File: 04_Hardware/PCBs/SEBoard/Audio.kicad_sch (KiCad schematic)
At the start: 20 parts, among them J22 53047-0210, U1 SC200EEMNA-E53-UGNDA, U100 PAM8302AASCR

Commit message: feat(schematic): add SE250B4 symbol to schematic (unchecked)
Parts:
- removed TP49, TP50, TP51: VBAT, TestPoint:TestPoint_Pad_D1.0mm, symbol SEBoard:TestPoint
- removed U1: SC200EEMNA-E53-UGNDA, SEBoard:SC200E_SC206E, symbol SEBoard:SC200E
- added C108: 10pF 50V, 000MCLib:CAPC1005X55N, symbol 000MCLib:GRM1555C1H100JA01D
- added C109, C65, C99: 100nF 10V, 000MCLib:CAPC1005X55N, symbol 000MCLib:GRM155R71A104KA01D
- added C63: 33pF 50V, 000MCLib:CAPC1005X55N, symbol 000MCLib:GRM1555C1H330JA01D
- added FB3: 110Ohm 1200mA, 000MCLib:BEADC1005X55N, symbol 000MCLib:74269242111
- added MK1: CMM-3729AT-42316-TR, 000MCLib:CMM3729AT42316TR, symbol 000MCLib:CMM-3729AT-42316-TR
- added R102: 0R, 000MCLib:RC0402N_YAG, symbol 000MCLib:RC0402JR-070RL
- added U5: SE250B4, 000MCLib:XCVR_SE250B4-NA, symbol 000MCLib:SE250B4
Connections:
- net GND: now also C108.2, C109.2, C63.2, R102.2
- net at C100.1: now also U5.BD6 (CDC_AUX_P)
- net at C101.1: now also U5.BE5 (CDC_AUX_M)
- new net: C108.1, C65.2, MK1.4 (OUTPUT)
- new net: C99.2, MK1.2 (GND_1), MK1.3 (GND_2), R102.1
- new net: C109.1, FB3.1, MK1.1 (VDD)
- new net MIC1_M: C99.1, U5.BD8 (CDC_IN1_M)
- new net MIC1_P: C63.1, C65.1, U5.BC7 (CDC_IN1_P)
- new net MIC_BIAS1: FB3.2, U5.BC9 (CDC_MIC_BIAS1)
- no-connect marks 12 -> 17
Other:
- note added: "Mic"

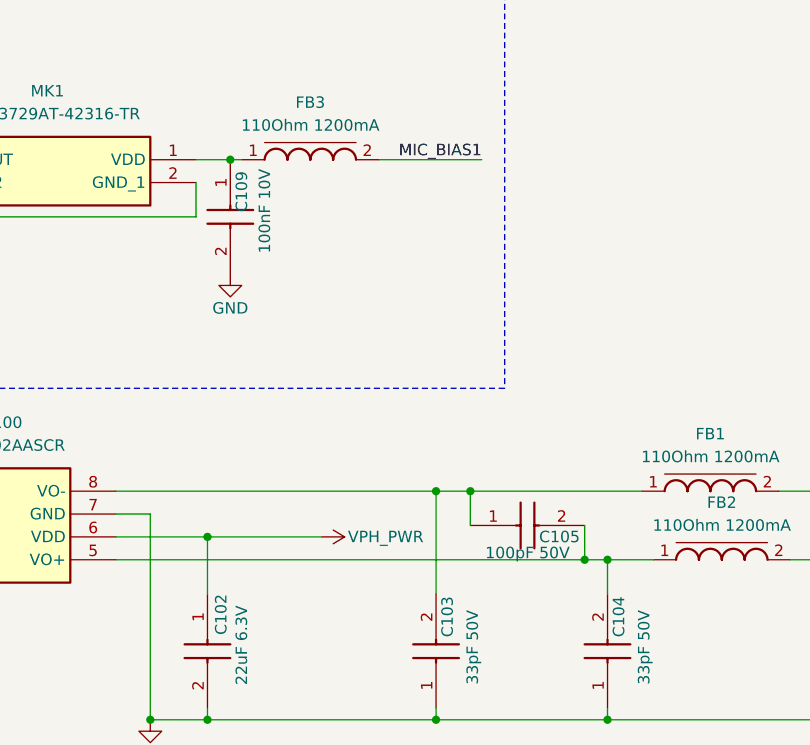
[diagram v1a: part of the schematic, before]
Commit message: feat: Updated schematic layout and moved new components to Layout
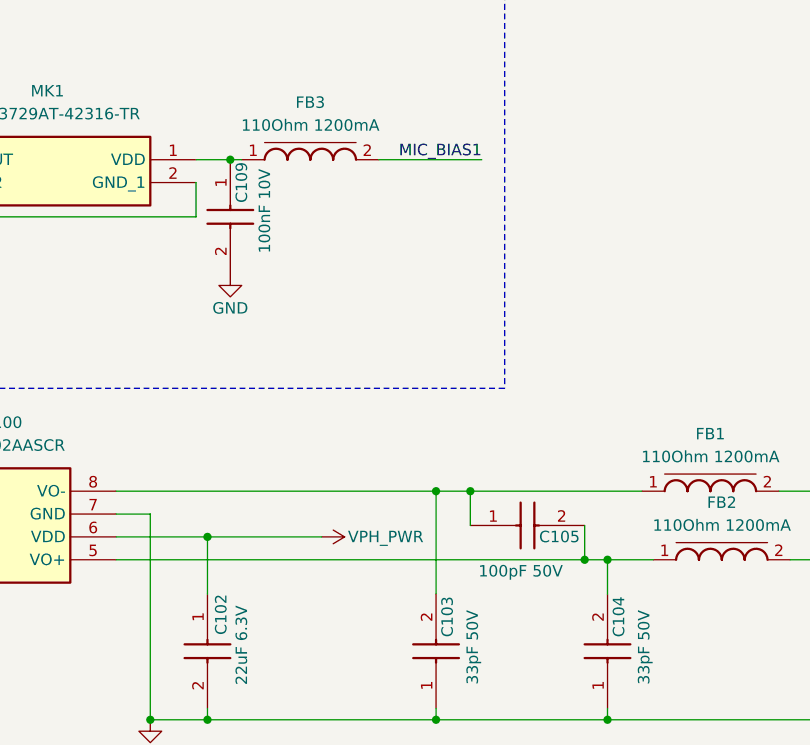
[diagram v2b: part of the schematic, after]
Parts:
- removed C105: 100pF 50V, SEBoard:CAPC1005X55N, symbol SEBoard:GRM1555C1H101JA01D
- added C105: 100pF 50V, 000MCLib:CAPC1005X55N, symbol 000MCLib:GRM1555C1H101JA01J
- C100, C101: footprint SEBoard:CAPC1005X55N -> 000MCLib:CAPC1005X55N; symbol SEBoard:GRM155R60J106ME15D -> 000MCLib:GRM155R60J106ME15D
- C102: footprint SEBoard:CAPC1005X55N -> 000MCLib:CAPC1005X55N; symbol SEBoard:GRM158R60J226ME01D -> 000MCLib:GRM158R60J226ME01D
- C103, C104, C106, C107: footprint SEBoard:CAPC1005X55N -> 000MCLib:CAPC1005X55N; symbol SEBoard:GRM1555C1H330JA01D -> 000MCLib:GRM1555C1H330JA01D
- FB1, FB2: footprint SEBoard:BEADC1005X55N -> 000MCLib:BEADC1005X55N; symbol SEBoard:74269242111 -> 000MCLib:74269242111
- J22: footprint SEBoard:530470210 -> 000MCLib:530470210; symbol SEBoard:53047-0210 -> 000MCLib:53047-0210
- LS1: symbol SEBoard:SPKM.15.8.A -> 000MCLib:SPKM.15.8.A
- R109, R110, R111: footprint SEBoard:RC0402N_YAG -> 000MCLib:RC0402N_YAG; symbol SEBoard:RC0402JR-0710KL -> 000MCLib:RC0402JR-0710KL
- U100: footprint SEBoard:SOP65P490X110-8N -> 000MCLib:SOP65P490X110-8N; symbol SEBoard:PAM8302AASCR -> 000MCLib:PAM8302AASCR
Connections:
- net at C103.2, FB1.1, U100.8 (VO-): now also C105.1
- net at C104.2, FB2.1, U100.5 (VO+): now also C105.2
